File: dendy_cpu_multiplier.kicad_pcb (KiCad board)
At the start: 2 copper layers, 15.2 x 51.1 mm, 12 parts, among them J1 CLK_IN, J2 CPU Connections, U1 74ACT74, U2 ICS501

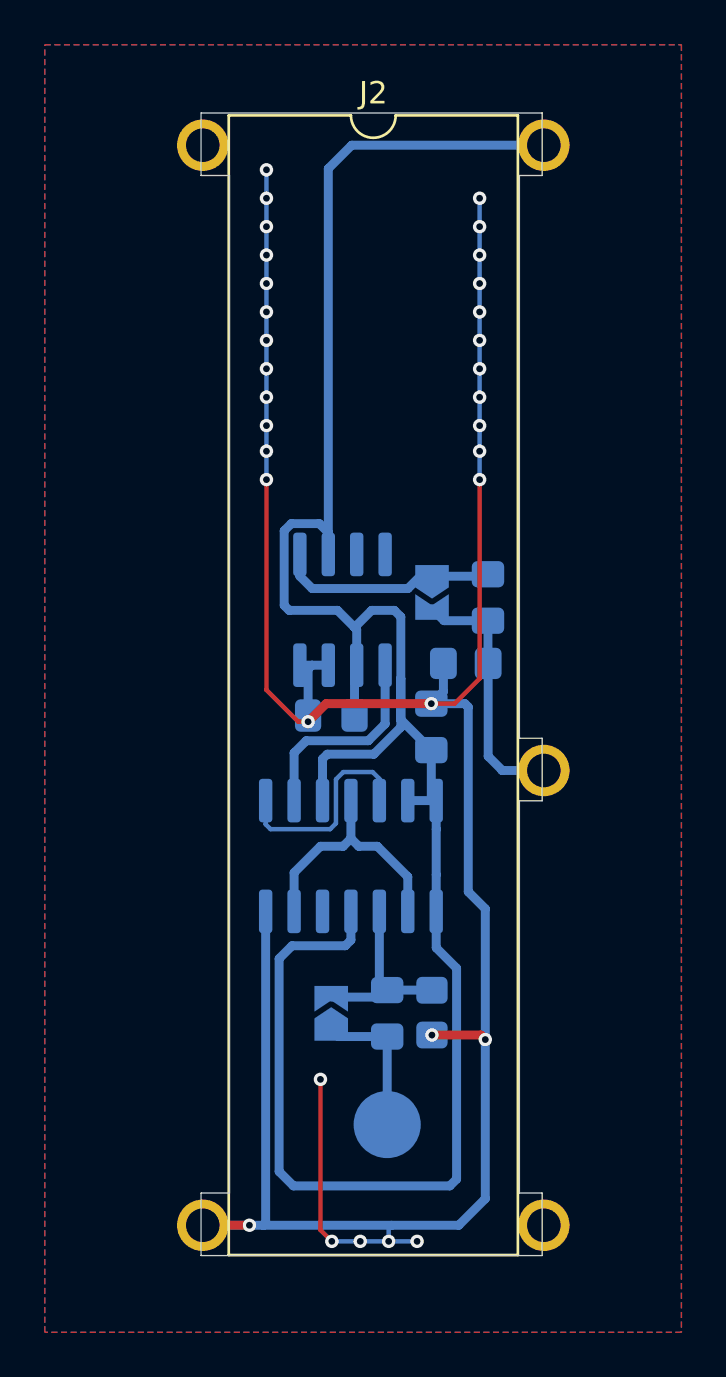
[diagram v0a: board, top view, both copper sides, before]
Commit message: Add some silkscreen tweaks
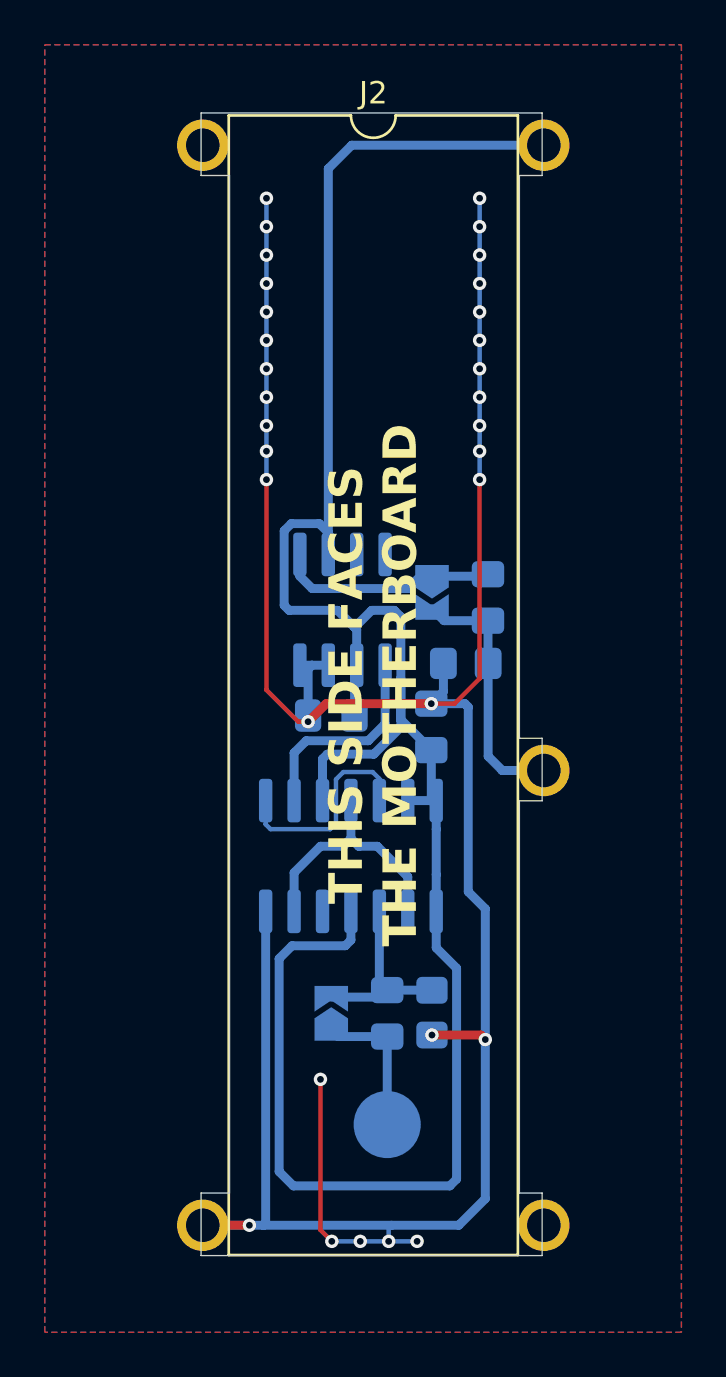
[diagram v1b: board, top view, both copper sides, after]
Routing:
- net GND: track 128.4 -> 127.1 mm, vias 33 -> 32
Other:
- board text added: "PIN 1"
- board text added: "Rev. 0"
- board text added: "THIS SIDE FACES THE MOTHERBOARD"
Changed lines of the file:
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@@
+	)
+	(gr_line
+		(start 142.113 52.451)
+		(end 140.97 52.451)
+		(stroke
+			(width 0.1)
+			(type default)
+		)
+		(layer "B.SilkS")
+	)
+	(gr_line
+		(start 140.97 51.943)
+		(end 140.335 52.451)
+		(stroke
+			(width 0.1)
+			(type default)
+		)
+		(layer "B.SilkS")
+	)
+	(gr_line
+		(start 140.335 52.451)
+		(end 140.97 52.959)
+		(stroke
+			(width 0.1)
+			(type default)
+		)
+		(layer "B.SilkS")
+	)
+	(gr_line
+		(start 140.97 52.959)
+		(end 140.97 52.451)
+		(stroke
+			(width 0.1)
+			(type default)
+		)
+		(layer "B.SilkS")
+	)
+	(gr_line
+		(start 140.97 52.451)
+		(end 140.97 51.943)
+		(stroke
+			(width 0.1)
+			(type default)
+		)
+		(layer "B.SilkS")
 	)
 	(gr_line
@@
 		(layer "Edge.Cuts")
 	)
+	(gr_text "THIS SIDE FACES\nTHE MOTHERBOARD"
+		(at 146.38 76.365 90)
+		(layer "F.SilkS")
+		(effects
+			(font
+				(size 1.5 1.5)
+				(thickness 0.3)
+				(bold yes)
+			)
+		)
+	)
+	(gr_text "PIN 1"
+		(at 146.685 52.451 0)
+		(layer "B.SilkS")
+		(effects
+			(font
+				(size 1 1)
+				(thickness 0.2)
+				(bold yes)
+			)
+			(justify left mirror)
+		)
+	)
 	(gr_text "DENDY CPU\n1.25x CLOCK\nMULTIPLIER"
-		(at 146.685 60.833 90)
+		(at 145.796 60.833 90)
 		(layer "B.SilkS")
 		(effects
@@
 		)
 	)
+	(gr_text "Rev. 0"
+		(at 149.098 60.96 90)
+		(layer "B.SilkS")
+		(effects
+			(font
+				(size 0.8 0.8)
+				(thickness 0.1)
+			)
+			(justify mirror)
+		)
+	)
 	(segment
 		(start 149.19 86.475)
@@
 	)
 	(via
-		(at 141.605 53.34)
-		(size 0.6)
-		(drill 0.3)
-		(layers "F.Cu" "B.Cu")
-		(free yes)
-		(net 2)
-	)
-	(via
 		(at 151.13 54.61)
 		(size 0.6)
@@
 		(layers "F.Cu" "B.Cu")
 		(free yes)
+		(net 2)
+	)
+	(segment
+		(start 141.605 54.61)
+		(end 141.605 67.183)
+		(width 0.2)
+		(layer "B.Cu")
 		(net 2)
 	)
@@
 	)
 	(segment
-		(start 141.605 53.34)
-		(end 141.605 67.183)
-		(width 0.2)
-		(layer "B.Cu")
-		(net 2)
-	)
-	(segment
 		(start 150.198 100.5)
 		(end 147.193 100.5)
@@
 	)
 	(zone
+		(net 0)
+		(net_name "")
+		(layer "F.Cu")
+		(hatch edge 0.5)
+		(connect_pads
+			(clearance 0)
+		)
+		(min_thickness 0.25)
+		(filled_areas_thickness no)
+		(keepout
+			(tracks allowed)
+			(vias allowed)
+			(pads allowed)
+			(copperpour not_allowed)
+			(footprints allowed)
+		)
+		(placement
+			(enabled no)
+			(sheetname "/")
+		)
+		(fill
+			(thermal_gap 0.5)
+			(thermal_bridge_width 0.5)
+		)
+		(polygon
+			(pts
+				(xy 156.718 78.613) (xy 156.718 81.788) (xy 151.003 81.788) (xy 151.003 78.613)
+			)
+		)
+	)
+	(zone
+		(net 0)
+		(net_name "")
+		(layer "F.Cu")
+		(hatch edge 0.5)
+		(connect_pads
+			(clearance 0)
+		)
+		(min_thickness 0.25)
+		(filled_areas_thickness no)
+		(keepout
+			(tracks allowed)
+			(vias allowed)
+			(pads allowed)
+			(copperpour not_allowed)
+			(footprints allowed)
+		)
+		(placement
+			(enabled no)
+			(sheetname "/")
+		)
+		(fill
+			(thermal_gap 0.5)
+			(thermal_bridge_width 0.5)
+		)
+		(polygon
+			(pts
+				(xy 141.605 50.8) (xy 141.605 53.975) (xy 135.89 53.975) (xy 135.89 50.8)
+			)
+		)
+	)
+	(zone
+		(net 0)
+		(net_name "")
+		(layer "F.Cu")
+		(hatch edge 0.5)
+		(connect_pads
+			(clearance 0)
+		)
+		(min_thickness 0.25)
+		(filled_areas_thickness no)
+		(keepout
+			(tracks allowed)
+			(vias allowed)
+			(pads allowed)
+			(copperpour not_allowed)
+			(footprints allowed)
+		)
+		(placement
+			(enabled no)
+			(sheetname "/")
+		)
+		(fill
+			(thermal_gap 0.5)
+			(thermal_bridge_width 0.5)
+		)
+		(polygon
+			(pts
+				(xy 156.718 98.933) (xy 156.718 102.108) (xy 151.003 102.108) (xy 151.003 98.933)
+			)
+		)
+	)
+	(zone
